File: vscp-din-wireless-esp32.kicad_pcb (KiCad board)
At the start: 2 copper layers, 64.8 x 51 mm, 18 parts, among them J1 Conn_Left_I2C, J2 Conn_Right_Power, J3 Conn_01x06, U1 ESP32-WROOM-32D

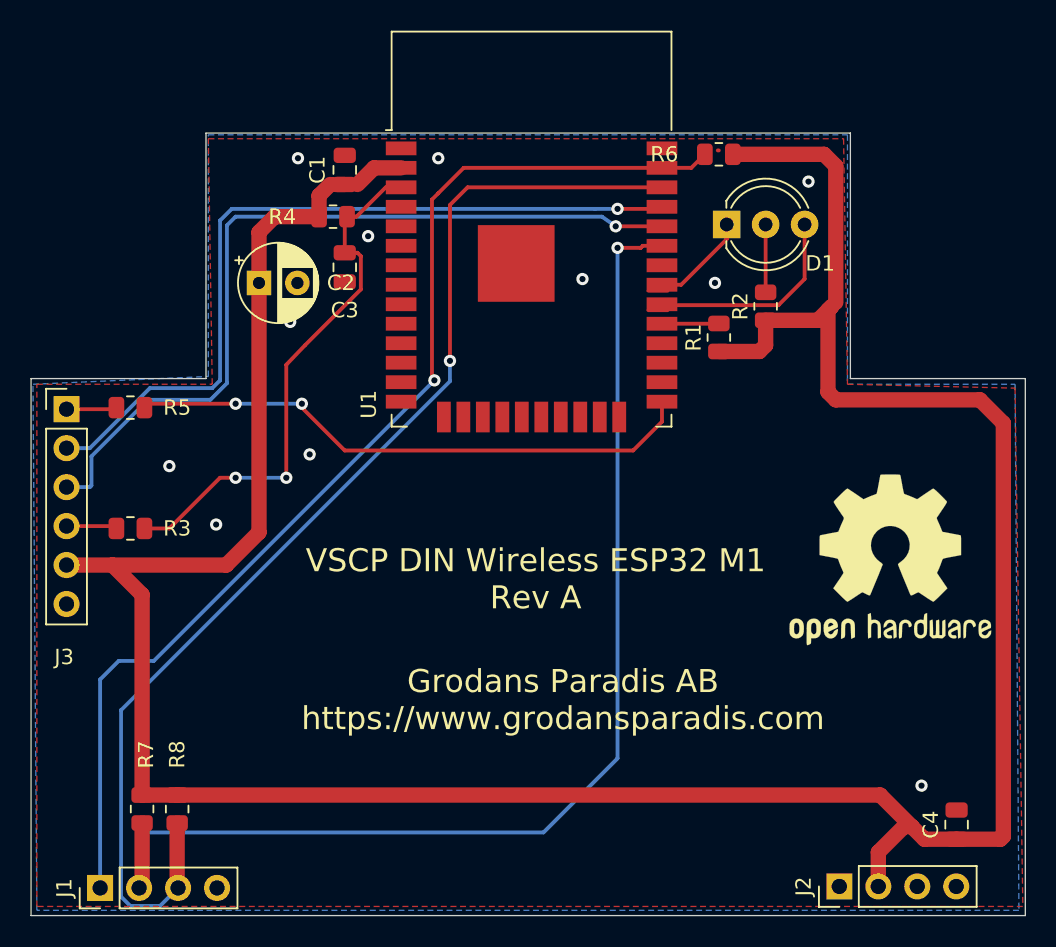
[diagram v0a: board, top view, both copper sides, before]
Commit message: srinked board to fit enclosure
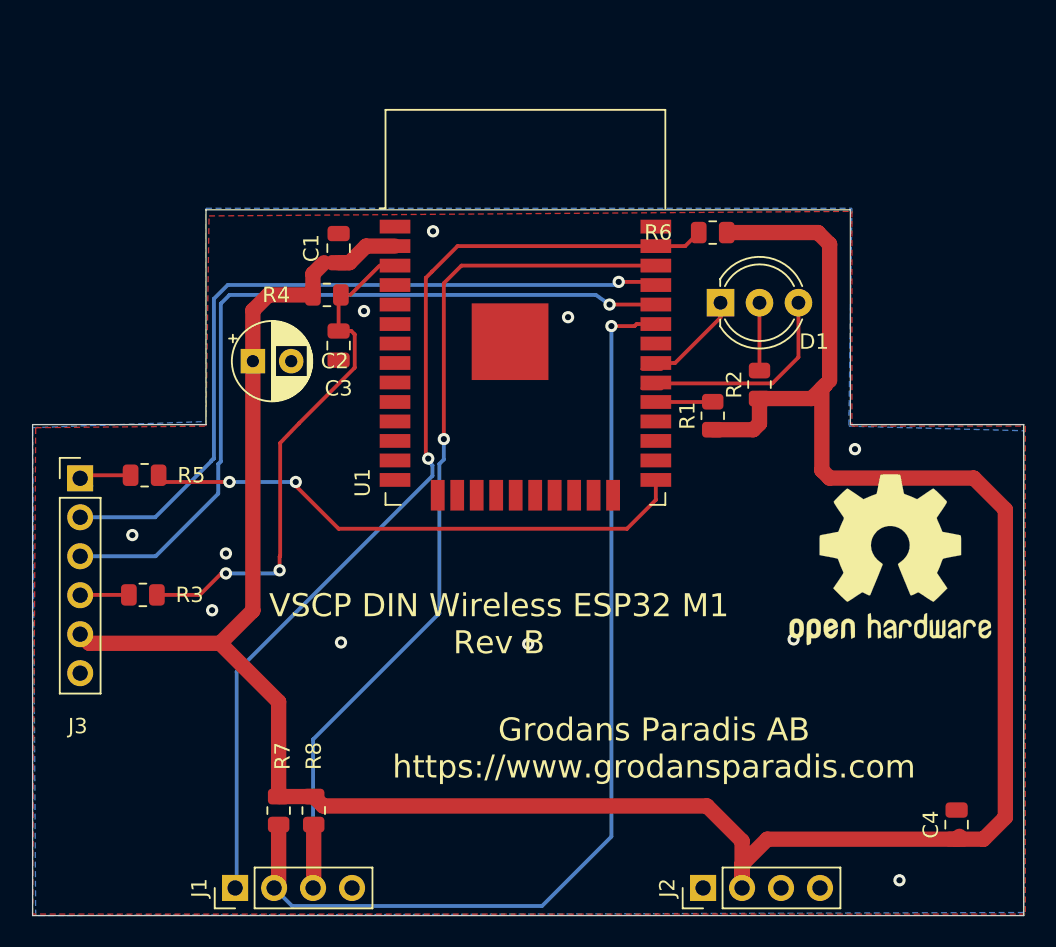
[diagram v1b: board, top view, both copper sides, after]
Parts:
- moved R8 8.90 mm to (134.1, 92.6)
- moved R7 8.90 mm to (131.8, 92.6)
- moved J2 8.88 mm to (159.5, 97.6)
- moved J1 8.80 mm to (129.0, 97.6)
- moved R2 5.12 mm to (163.2, 64.8)
- moved C1 5.12 mm to (135.7, 55.9)
- moved C2 5.12 mm to (130.2, 63.3)
- moved C3 5.12 mm to (135.7, 62.2)
- moved D1 5.12 mm to (160.6, 59.5)
- moved R1 5.12 mm to (160.1, 66.8)
- moved R4 5.12 mm to (135.0, 58.9)
- moved R6 5.12 mm to (160.1, 54.9)
- moved U1 5.12 mm to (147.9, 62.8)
- moved J3 4.59 mm to (118.9, 70.9)
- moved R5 4.50 mm to (123.1, 70.7)
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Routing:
- net VCC: track 193.8 -> 173.7 mm
- net /scl: track 77.0 -> 61.4 mm
- net /sda: track 77.1 -> 64.6 mm
- net /irq: track 74.3 -> 64.3 mm
- net /reset: track 34.9 -> 32.1 mm
- net /RXD: track 53.5 -> 51.9 mm
- net /TXD: track 51.4 -> 50.1 mm
- net Net-(R5-Pad1): track 37.3 -> 36.1 mm
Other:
- board size 64.8 x 51 mm -> 64.6 x 46 mm
- board text added: "VSCP DIN Wireless ESP32 M1 Rev B"
- board text removed: "VSCP DIN Wireless ESP32 M1 Rev A"
